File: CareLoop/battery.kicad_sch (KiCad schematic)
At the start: 14 parts, among them J1_Battery1 Conn_01x02_Pin, J2 USB_B_Micro, U4 MCP1700x-330xxMB, U5 TP4056-42-ESOP8

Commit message: update PCB
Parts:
- C40, C42, C43: JLCPCB Part#(optional) (none) -> C88945
- C41: JLCPCB Part#(optional) (none) -> C15525
- D40, D41: JLCPCB Part#(optional) (none) -> C20608782
- J1_Battery1, JP2_MPU1: footprint Connector_PinHeader_1.00mm:PinHeader_1x02_P1.00mm_Vertical -> Connector_PinHeader_2.00mm:PinHeader_1x02_P2.00mm_Vertical; now not fitted
- J2: JLCPCB Part#(optional) (none) -> C428495
- R40, R41: JLCPCB Part#(optional) (none) -> C11702
- R42: JLCPCB Part#(optional) (none) -> C25545
- U4: JLCPCB Part#(optional) (none) -> C39051
- U5: JLCPCB Part#(optional) (none) -> C382139
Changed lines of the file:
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@@
+			)
+		)
+		(property "JLCPCB Part#(optional)" "C11702"
+			(at 76.2 77.47 0)
+			(effects
+				(font
+					(size 1.27 1.27)
+				)
+				(hide yes)
 			)
 		)
@@
 			)
 		)
+		(property "JLCPCB Part#(optional)" "C15525"
+			(at 132.08 87.63 0)
+			(effects
+				(font
+					(size 1.27 1.27)
+				)
+				(hide yes)
+			)
+		)
 		(pin "1"
 		)
@@
 		(in_bom yes)
 		(on_board yes)
-		(dnp no)
+		(dnp yes)
 		(fields_autoplaced yes)
 		(property "Reference" "JP2_MPU1"
@@
 			)
 		)
-		(property "Footprint" "Connector_PinHeader_1.00mm:PinHeader_1x02_P1.00mm_Vertical"
+		(property "Footprint" "Connector_PinHeader_2.00mm:PinHeader_1x02_P2.00mm_Vertical"
 			(at 143.51 67.31 0)
 			(effects
@@
 			)
 		)
+		(property "JLCPCB Part#(optional)" ""
+			(at 143.51 67.31 0)
+			(effects
+				(font
+					(size 1.27 1.27)
+				)
+				(hide yes)
+			)
+		)
 		(pin "2"
 		)
@@
 			)
 		)
+		(property "JLCPCB Part#(optional)" "C382139"
+			(at 110.49 88.9 0)
+			(effects
+				(font
+					(size 1.27 1.27)
+				)
+				(hide yes)
+			)
+		)
 		(pin "2"
 		)
@@
 			)
 		)
+		(property "JLCPCB Part#(optional)" "C39051"
+			(at 154.94 80.01 0)
+			(effects
+				(font
+					(size 1.27 1.27)
+				)
+				(hide yes)
+			)
+		)
 		(pin "2"
 		)
@@
 			)
 		)
+		(property "JLCPCB Part#(optional)" "C88945"
+			(at 170.18 85.09 0)
+			(effects
+				(font
+					(size 1.27 1.27)
+				)
+				(hide yes)
+			)
+		)
 		(pin "1"
 		)
@@
 			)
 		)
+		(property "JLCPCB Part#(optional)" "C88945"
+			(at 138.43 85.09 0)
+			(effects
+				(font
+					(size 1.27 1.27)
+				)
+				(hide yes)
+			)
+		)
 		(pin "1"
 		)
@@
 			)
 		)
+		(property "JLCPCB Part#(optional)" "C20608782"
+			(at 88.9 85.09 90)
+			(effects
+				(font
+					(size 1.27 1.27)
+				)
+				(hide yes)
+			)
+		)
 		(pin "1"
 		)
@@
 			)
 		)
+		(property "JLCPCB Part#(optional)" "C88945"
+			(at 121.92 68.58 0)
+			(effects
+				(font
+					(size 1.27 1.27)
+				)
+				(hide yes)
+			)
+		)
 		(pin "1"
 		)
@@
 			)
 		)
+		(property "JLCPCB Part#(optional)" "C20608782"
+			(at 76.2 85.09 90)
+			(effects
+				(font
+					(size 1.27 1.27)
+				)
+				(hide yes)
+			)
+		)
 		(pin "1"
 		)
@@
 			)
 		)
+		(property "JLCPCB Part#(optional)" "C11702"
+			(at 88.9 77.47 0)
+			(effects
+				(font
+					(size 1.27 1.27)
+				)
+				(hide yes)
+			)
+		)
 		(pin "2"
 		)
@@
 			)
 		)
+		(property "JLCPCB Part#(optional)" "C428495"
+			(at 58.42 66.04 0)
+			(effects
+				(font
+					(size 1.27 1.27)
+				)
+				(hide yes)
+			)
+		)
 		(pin "1"
 		)
@@
 		(in_bom yes)
 		(on_board yes)
-		(dnp no)
+		(dnp yes)
 		(fields_autoplaced yes)
 		(property "Reference" "J1_Battery1"
@@
 			)
 		)
-		(property "Footprint" "Connector_PinHeader_1.00mm:PinHeader_1x02_P1.00mm_Vertical"
+		(property "Footprint" "Connector_PinHeader_2.00mm:PinHeader_1x02_P2.00mm_Vertical"
 			(at 140.97 54.61 0)
 			(effects
@@
 			)
 		)
+		(property "JLCPCB Part#(optional)" ""
+			(at 140.97 54.61 90)
+			(effects
+				(font
+					(size 1.27 1.27)
+				)
+				(hide yes)
+			)
+		)
 		(pin "1"
 		)
@@
 			(at 125.73 95.25 0)
 			(effects
+				(font
+					(size 1.27 1.27)
+				)
+				(hide yes)
+			)
+		)
+		(property "JLCPCB Part#(optional)" "C25545"
+			(at 125.73 95.25 0)
+			(effects

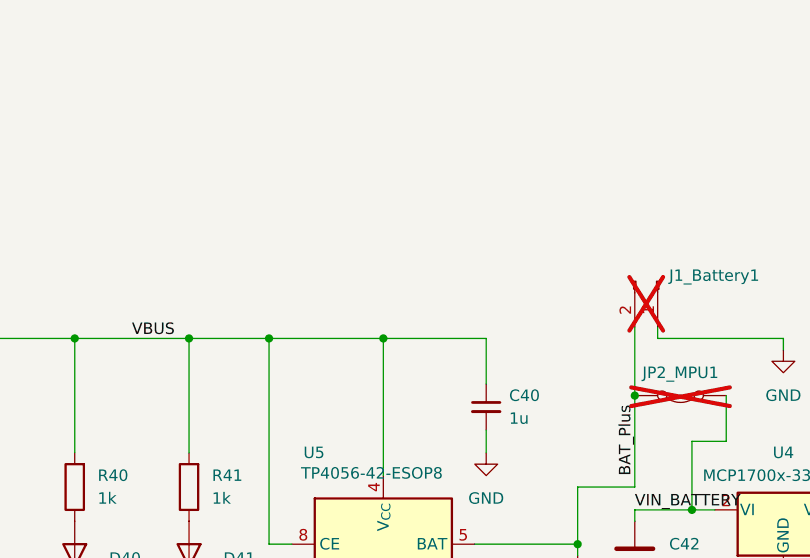
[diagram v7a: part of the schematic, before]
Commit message: update Voltagedevider
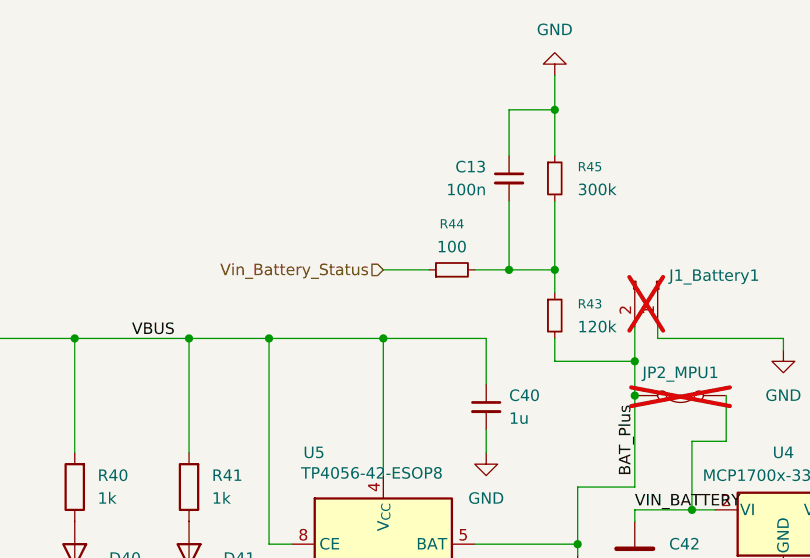
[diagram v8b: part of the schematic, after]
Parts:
- added C13: 100n, Capacitor_SMD:C_0201_0603Metric_Pad0.64x0.40mm_HandSolder, symbol Device:C_Small
- added R43: 120k, Resistor_SMD:R_0402_1005Metric_Pad0.72x0.64mm_HandSolder, symbol Device:R_Small
- added R44: 100, Resistor_SMD:R_0402_1005Metric_Pad0.72x0.64mm_HandSolder, symbol Device:R_Small
- added R45: 300k, Resistor_SMD:R_0402_1005Metric_Pad0.72x0.64mm_HandSolder, symbol Device:R_Small
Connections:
- net BAT_Plus: now also R43.2
- net GND: now also C13.1, R45.1
- new net: C13.2, R43.1, R44.2, R45.2
- new net Vin_Battery_Status: R44.1
